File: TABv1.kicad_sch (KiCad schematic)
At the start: 40 parts, among them J10 Conn_02x03_Odd_Even, J11 Conn_02x06_Counter_Clockwise, J6 Conn_02x06_Counter_Clockwise, J9 Conn_02x03_Odd_Even, Q3 DMN2040U, SW2 RESET, U1 RP2350B-QFN80, Y1 12MHz

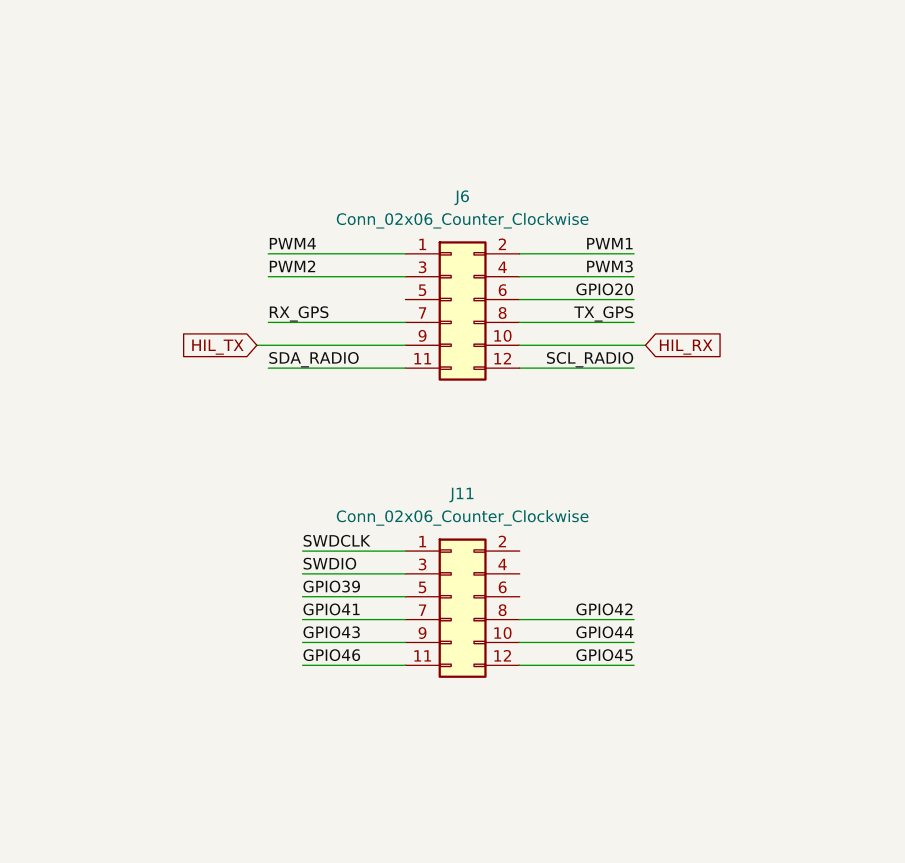
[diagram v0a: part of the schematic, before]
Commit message: fixed the connectors, rearranged sensors and fixed a bit the silkscreen
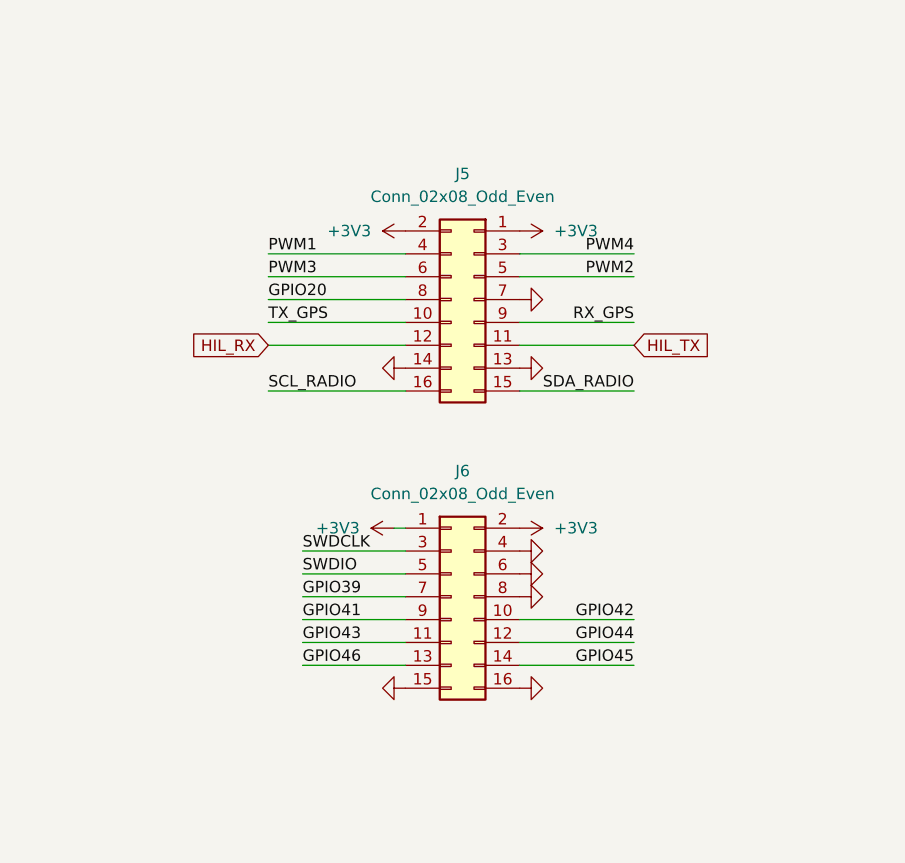
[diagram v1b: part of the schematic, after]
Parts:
- removed J11, J6: Conn_02x06_Counter_Clockwise, Connector_PinHeader_2.54mm:PinHeader_2x06_P2.54mm_Vertical, symbol Connector_Generic:Conn_02x06_Odd_Even
- added J5, J6: Conn_02x08_Odd_Even, Connector_PinHeader_2.54mm:PinHeader_2x08_P2.54mm_Vertical, symbol Connector_Generic:Conn_02x08_Odd_Even
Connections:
- net +3V3: now also J5.1 (Pin_1), J5.2 (Pin_2), J6.1 (Pin_1), J6.2 (Pin_2)
- net GND: now also J5.13 (Pin_13), J5.14 (Pin_14), J5.7 (Pin_7), J6.15 (Pin_15), J6.16 (Pin_16), J6.4 (Pin_4), J6.6 (Pin_6), J6.8 (Pin_8)
- net GPIO20: now also J5.8 (Pin_8)
- net GPIO39: now also J6.7 (Pin_7)
- net GPIO41: now also J6.9 (Pin_9)
- net GPIO42: now also J6.10 (Pin_10)
- net GPIO43: now also J6.11 (Pin_11)
- net GPIO44: now also J6.12 (Pin_12)
- net GPIO45: now also J6.14 (Pin_14)
- net GPIO46: now also J6.13 (Pin_13)
- net HIL_RX: now also J5.12 (Pin_12)
- net HIL_TX: now also J5.11 (Pin_11)
- net PWM1: now also J5.4 (Pin_4)
- net PWM2: now also J5.5 (Pin_5)
- net PWM3: now also J5.6 (Pin_6)
- net PWM4: now also J5.3 (Pin_3)
- net RX_GPS: now also J5.9 (Pin_9)
- net SCL_RADIO: now also J5.16 (Pin_16)
- net SDA_RADIO: now also J5.15 (Pin_15)
- net SWDCLK: now also J6.3 (Pin_3)
- net SWDIO: now also J6.5 (Pin_5)
- net TX_GPS: now also J5.10 (Pin_10)

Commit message: small fixes, started working on the backpack
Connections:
- net GND: no longer J6.4 (Pin_4), J6.6 (Pin_6), J6.8 (Pin_8)
- net PPS: now also J6.4 (Pin_4)
- net RESET: now also J6.8 (Pin_8)
- new net BOOTSEL: J6.6 (Pin_6)
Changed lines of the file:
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@@
 		)
 	)
+	(wire
+		(pts
+			(xy 267.97 115.57) (xy 255.27 115.57)
+		)
+		(stroke
+			(width 0)
+			(type default)
+		)
+	)
 	(polyline
 		(pts
@@
 	(wire
 		(pts
+			(xy 267.97 110.49) (xy 255.27 110.49)
+		)
+		(stroke
+			(width 0)
+			(type default)
+		)
+	)
+	(wire
+		(pts
 			(xy 129.54 106.68) (xy 165.1 106.68)
 		)
@@
 	(wire
 		(pts
+			(xy 267.97 113.03) (xy 255.27 113.03)
+		)
+		(stroke
+			(width 0)
+			(type default)
+		)
+	)
+	(wire
+		(pts
 			(xy 58.42 241.3) (xy 60.96 241.3)
 		)
@@
 		)
 	)
+	(label "RESET"
+		(at 267.97 115.57 180)
+		(effects
+			(font
+				(size 1.27 1.27)
+			)
+			(justify right bottom)
+		)
+	)
 	(label "SD0"
 		(at 39.37 77.47 0)
@@
 		)
 	)
+	(global_label "BOOTSEL"
+		(shape input)
+		(at 267.97 113.03 0)
+		(fields_autoplaced yes)
+		(effects
+			(font
+				(size 1.27 1.27)
+			)
+			(justify left)
+		)
+		(property "Intersheetrefs" "${INTERSHEET_REFS}"
+			(at 279.2404 113.03 0)
+			(effects
+				(font
+					(size 1.27 1.27)
+				)
+				(justify left)
+				(hide yes)
+			)
+		)
+	)
 	(global_label "PPS"
 		(shape input)
@@
 		)
 	)
+	(global_label "PPS"
+		(shape input)
+		(at 267.97 110.49 0)
+		(fields_autoplaced yes)
+		(effects
+			(font
+				(size 1.27 1.27)
+			)
+			(justify left)
+		)
+		(property "Intersheetrefs" "${INTERSHEET_REFS}"
+			(at 274.7047 110.49 0)
+			(effects
+				(font
+					(size 1.27 1.27)
+				)
+				(justify left)
+				(hide yes)
+			)
+		)
+	)
 	(global_label "HIL_RX"
 		(shape input)
@@
 	(symbol
 		(lib_id "power:GND")
-		(at 255.27 110.49 90)
-		(unit 1)
-		(exclude_from_sim no)
-		(in_bom yes)
-		(on_board yes)
-		(dnp no)
-		(fields_autoplaced yes)
-		(property "Reference" "#PWR0143"
-			(at 261.62 110.49 0)
-			(effects
-				(font
-					(size 1.27 1.27)
-				)
-				(hide yes)
-			)
-		)
-		(property "Value" "GND"
-			(at 259.08 110.4901 90)
-			(effects
-				(font
-					(size 1.27 1.27)
-				)
-				(justify right)
-				(hide yes)
-			)
-		)
-		(property "Footprint" ""
-			(at 255.27 110.49 0)
-			(effects
-				(font
-					(size 1.27 1.27)
-				)
-				(hide yes)
-			)
-		)
-		(property "Datasheet" ""
-			(at 255.27 110.49 0)
-			(effects
-				(font
-					(size 1.27 1.27)
-				)
-				(hide yes)
-			)
-		)
-		(property "Description" "Power symbol creates a global label with name \"GND\" , ground"
-			(at 255.27 110.49 0)
-			(effects
-				(font
-					(size 1.27 1.27)
-				)
-				(hide yes)
-			)
-		)
-		(pin "1"
-		)
-		(instances
-			(project "TABv1"
-				(path "/105f6e80-8e20-4d56-8eb3-6fa826818670"
-					(reference "#PWR0143")
-					(unit 1)
-				)
-			)
-		)
-	)
-	(symbol
-		(lib_id "power:GND")
 		(at 266.7 242.57 90)
 		(unit 1)
@@
 	(symbol
 		(lib_id "power:GND")
-		(at 255.27 113.03 90)
-		(unit 1)
-		(exclude_from_sim no)
-		(in_bom yes)
-		(on_board yes)
-		(dnp no)
-		(fields_autoplaced yes)
-		(property "Reference" "#PWR0142"
-			(at 261.62 113.03 0)
-			(effects
-				(font
-					(size 1.27 1.27)
-				)
-				(hide yes)
-			)
-		)
-		(property "Value" "GND"
-			(at 259.08 113.0301 90)
-			(effects
-				(font
-					(size 1.27 1.27)
-				)
-				(justify right)
-				(hide yes)
-			)
-		)
-		(property "Footprint" ""
-			(at 255.27 113.03 0)
-			(effects
-				(font
-					(size 1.27 1.27)
-				)
-				(hide yes)
-			)
-		)
-		(property "Datasheet" ""
-			(at 255.27 113.03 0)
-			(effects
-				(font
-					(size 1.27 1.27)
-				)
-				(hide yes)
-			)
-		)
-		(property "Description" "Power symbol creates a global label with name \"GND\" , ground"
-			(at 255.27 113.03 0)
-			(effects
-				(font
-					(size 1.27 1.27)
-				)
-				(hide yes)
-			)
-		)
-		(pin "1"
-		)
-		(instances
-			(project "TABv1"
-				(path "/105f6e80-8e20-4d56-8eb3-6fa826818670"
-					(reference "#PWR0142")
-					(unit 1)
-				)
-			)
-		)
-	)
-	(symbol
-		(lib_id "power:GND")
 		(at 255.27 82.55 90)
 		(unit 1)
@@
 					(unit 1)
 				)
-			)
-		)
-	)
-	(symbol
-		(lib_id "power:GND")
-		(at 255.27 115.57 90)
-		(unit 1)
-		(exclude_from_sim no)
-		(in_bom yes)
-		(on_board yes)
-		(dnp no)
-		(fields_autoplaced yes)
-		(property "Reference" "#PWR0141"
-			(at 261.62 115.57 0)
-			(effects
-				(font
-					(size 1.27 1.27)
-				)
-				(hide yes)
-			)
-		)
-		(property "Value" "GND"
-			(at 259.08 115.5701 90)
-			(effects
-				(font
-					(size 1.27 1.27)
-				)
-				(justify right)
-				(hide yes)
-			)
-		)
-		(property "Footprint" ""
-			(at 255.27 115.57 0)
-			(effects
-				(font
-					(size 1.27 1.27)
-				)
-				(hide yes)
-			)
-		)
-		(property "Datasheet" ""
-			(at 255.27 115.57 0)
-			(effects
-				(font
-					(size 1.27 1.27)
-				)
-				(hide yes)
-			)
-		)
-		(property "Description" "Power symbol creates a global label with name \"GND\" , ground"
-			(at 255.27 115.57 0)
-			(effects
-				(font
-					(size 1.27 1.27)
-				)
-				(hide yes)
-			)
-		)
-		(pin "1"
-		)
-		(instances
-			(project "TABv1"
-				(path "/105f6e80-8e20-4d56-8eb3-6fa826818670"
-					(reference "#PWR0141")
-					(unit 1)
-				)
